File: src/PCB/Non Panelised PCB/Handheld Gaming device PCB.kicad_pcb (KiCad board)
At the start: 2 copper layers, 337.8 x 81.8 mm, 63 parts, among them J1 Conn_02x20_Odd_Even, J10 FCC Connector Left Board, J11 FCC Connector Right Board, J12 FCC Connector Right Board, J13 FCC Connector Left Board, J2 TP4056_Module, J3 Joystick_Left, J4 Joystick_Right, J5 Display_5V, J6 Speaker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

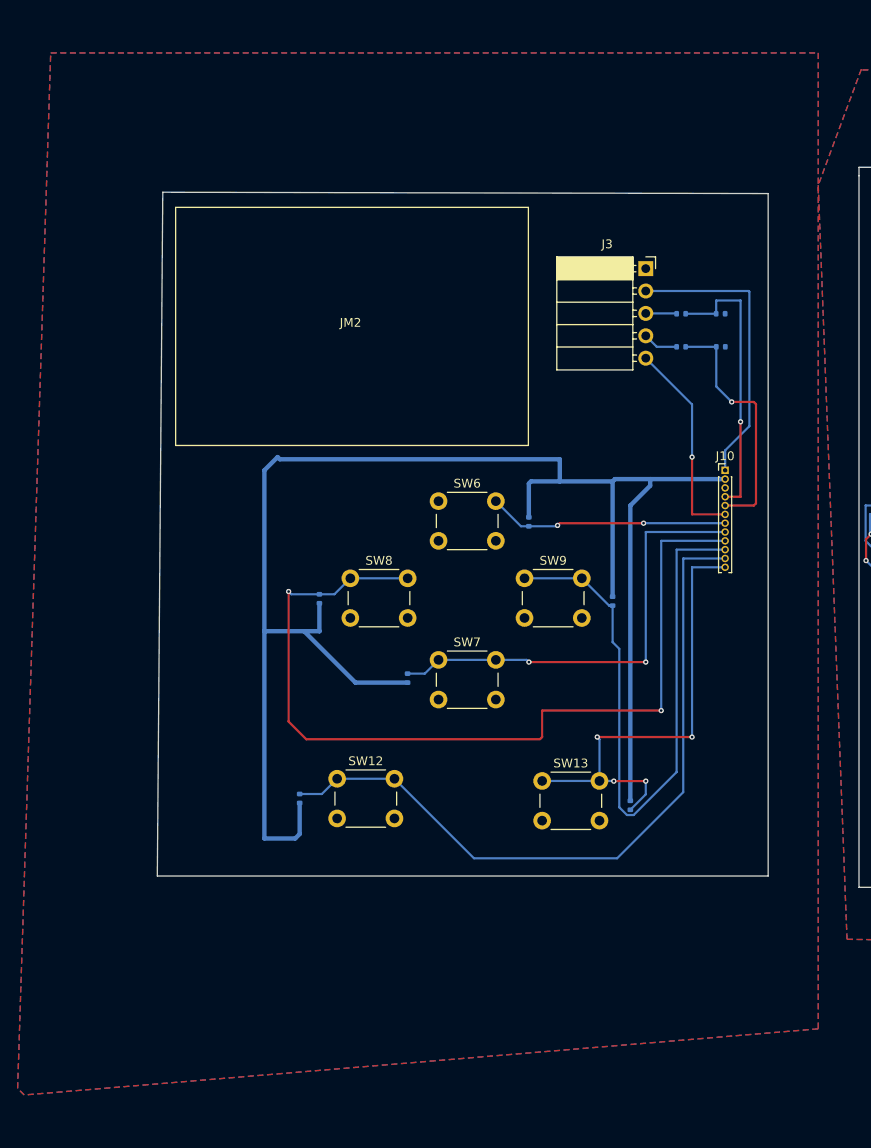
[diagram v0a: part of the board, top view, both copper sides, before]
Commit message: fixed errors in like the PCB that i just now noticed
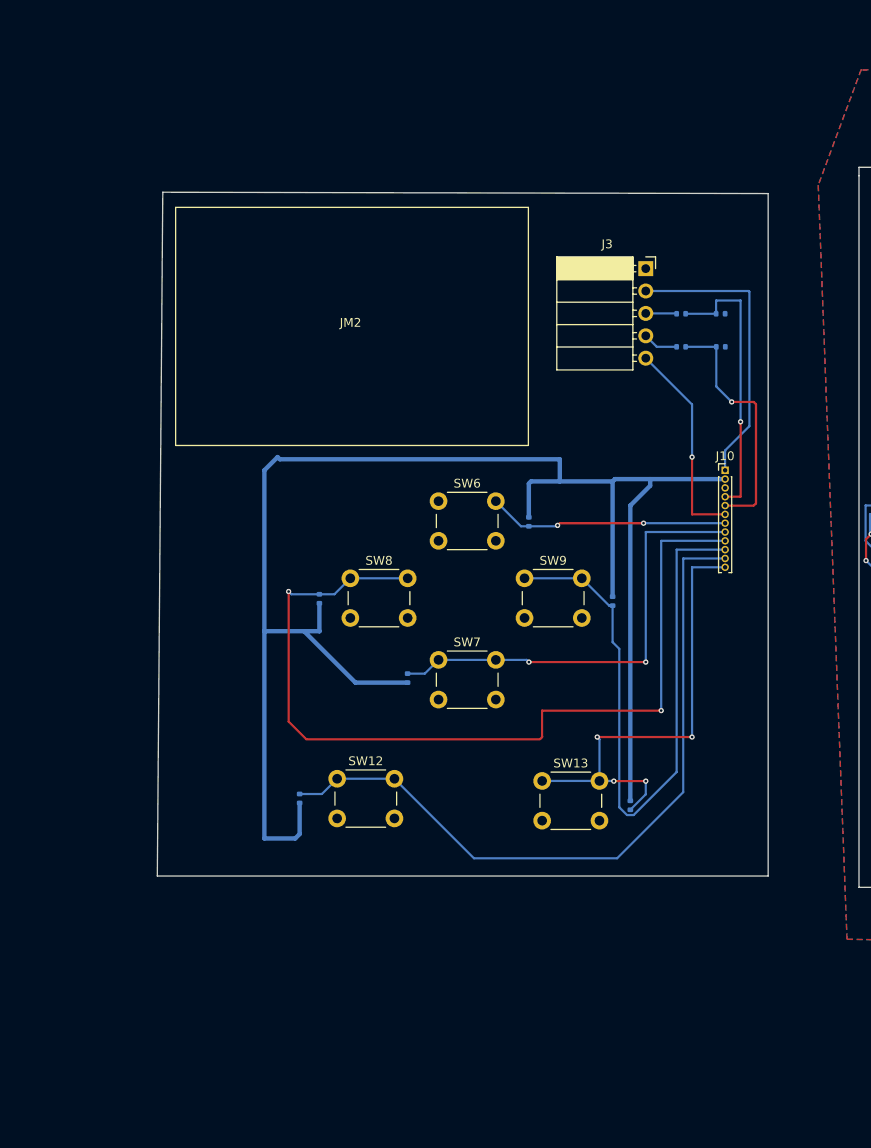
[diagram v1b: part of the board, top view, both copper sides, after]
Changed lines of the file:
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@@
-		)
-	)
-	(zone
-		(net "GND")
-		(layers "F.Cu" "B.Cu")
-		(hatch edge 0.5)
-		(priority 1)
-		(connect_pads
-			(clearance 0.5)
-		)
-		(min_thickness 0.25)
-		(fill yes
-			(thermal_gap 0.5)
-			(thermal_bridge_width 0.5)
-			(island_removal_mode 0)
-		)
-		(polygon
-			(pts
-				(xy 286.59 298.35) (xy 290.34 180.93) (xy 377.38 180.93) (xy 377.38 291.6) (xy 287.34 299.1)
-			)
 		)
 	)
